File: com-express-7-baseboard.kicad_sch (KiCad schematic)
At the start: 0 parts

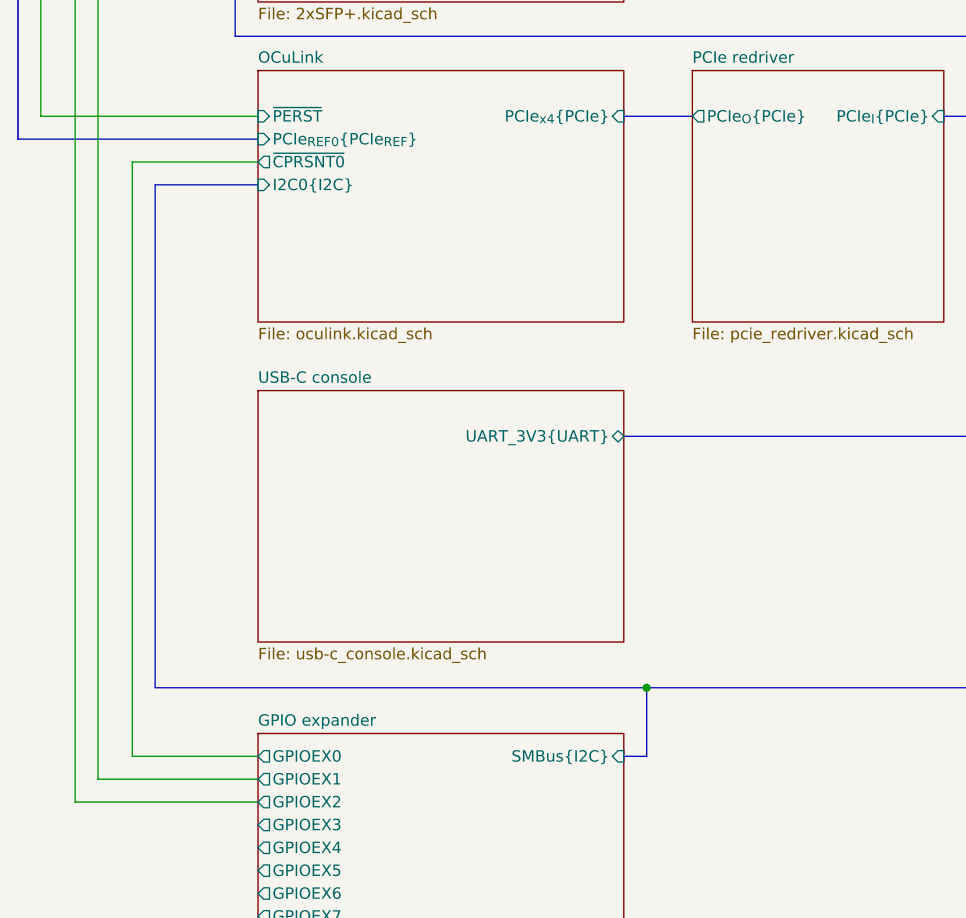
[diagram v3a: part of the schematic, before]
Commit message: [#57056] Add PCIe redriver for OCuLink
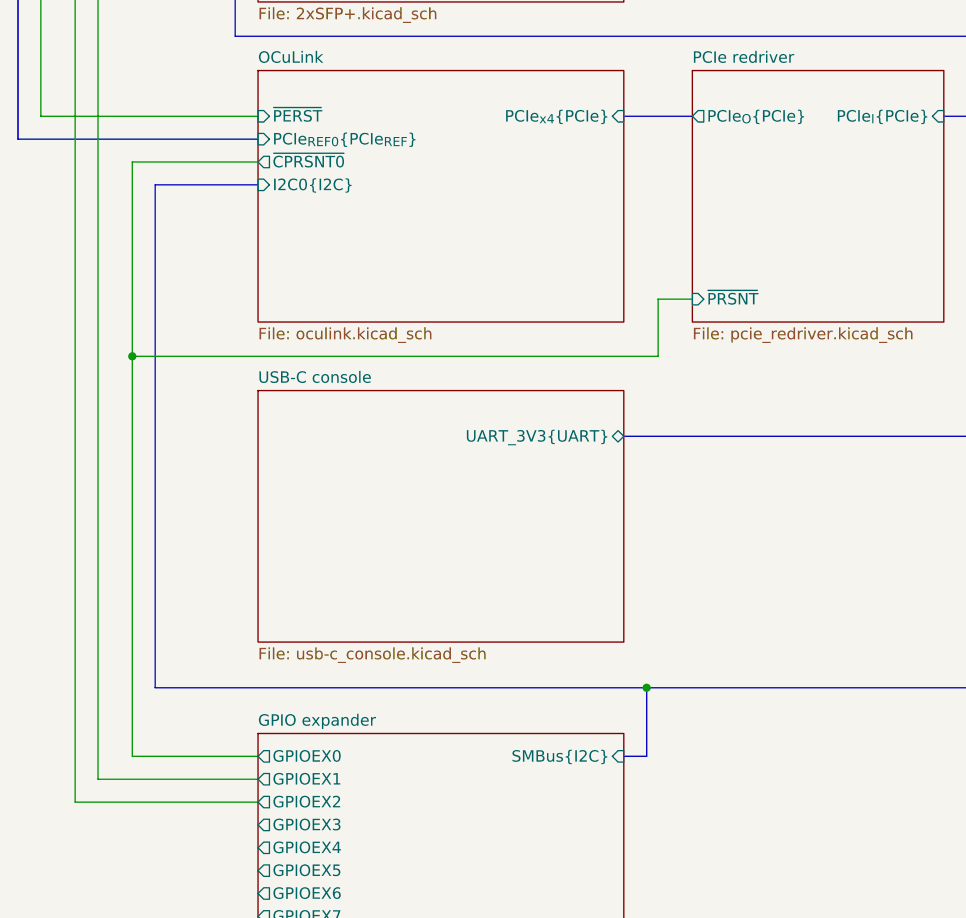
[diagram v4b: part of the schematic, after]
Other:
- sheet PCIe redriver ports: added ~{PRSNT}; removed none
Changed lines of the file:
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@@
   (junction (at 325.12 101.6) (diameter 0) (color 0 0 0 0)
+  )
+  (junction (at 64.77 171.45) (diameter 0) (color 0 0 0 0)
   )
   (junction (at 121.92 127) (diameter 0) (color 0 0 0 0)
@@
     (stroke (width 0) (type default))
   )
+  (wire (pts (xy 64.77 171.45) (xy 64.77 215.9))
+    (stroke (width 0) (type default))
+  )
   (bus (pts (xy 78.74 147.32) (xy 52.07 147.32))
     (stroke (width 0) (type default))
@@
     (stroke (width 0) (type default) (color 0 0 255 1))
   )
+  (wire (pts (xy 64.77 171.45) (xy 123.19 171.45))
+    (stroke (width 0) (type default))
+  )
   (bus (pts (xy 335.28 106.68) (xy 335.28 27.94))
     (stroke (width 0) (type default))
@@
     (stroke (width 0) (type default) (color 255 0 0 1))
   )
+  (wire (pts (xy 123.19 165.1) (xy 127 165.1))
+    (stroke (width 0) (type default))
+  )
   (wire (pts (xy 325.12 137.16) (xy 322.58 137.16))
     (stroke (width 0) (type default))
@@
     (stroke (width 0) (type default))
   )
+  (wire (pts (xy 123.19 171.45) (xy 123.19 165.1))
+    (stroke (width 0) (type default))
+  )
   (bus (pts (xy 119.38 215.9) (xy 121.92 215.9))
     (stroke (width 0) (type default))
@@
     (stroke (width 0) (type default))
   )
-  (wire (pts (xy 64.77 149.86) (xy 64.77 215.9))
+  (wire (pts (xy 64.77 149.86) (xy 64.77 171.45))
     (stroke (width 0) (type default))
   )
@@
       (effects (font (size 1.27 1.27)) (justify left))
     )
+    (pin "~{PRSNT}" input (at 127 165.1 180)
+      (effects (font (size 1.27 1.27)) (justify left))
+    )

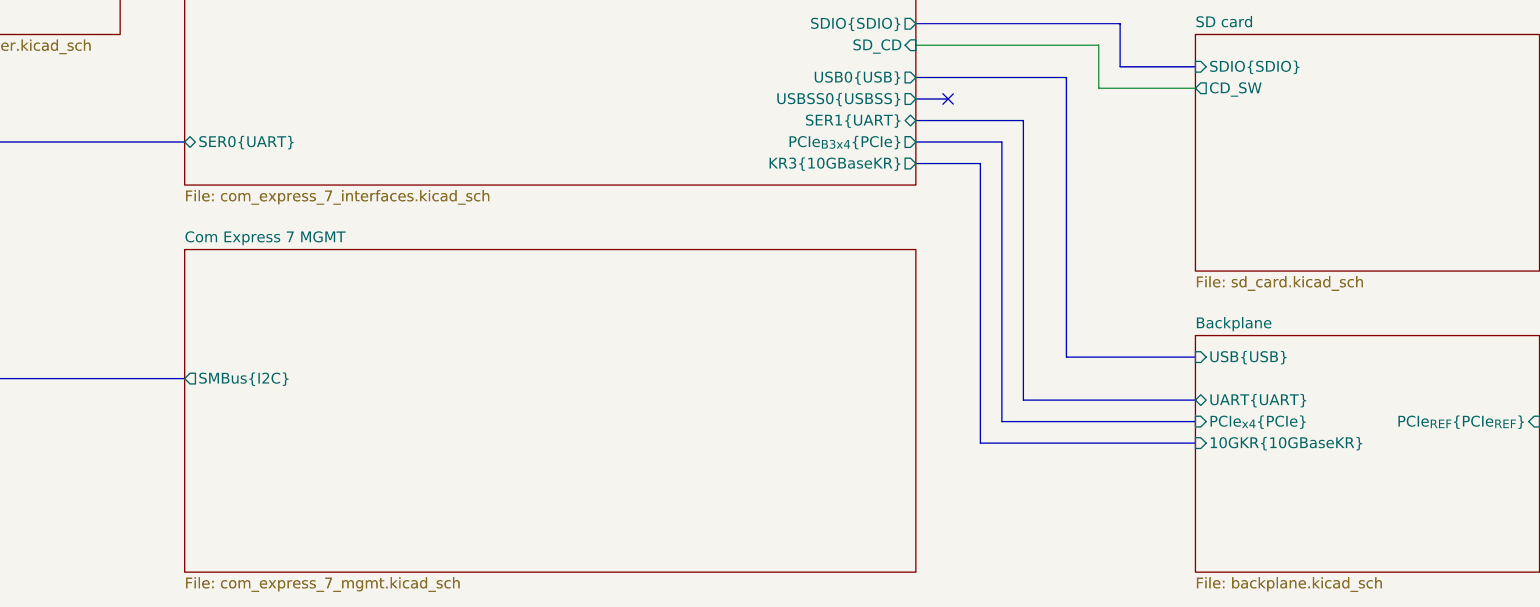
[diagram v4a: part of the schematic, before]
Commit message: [#57056] Add backplane connector
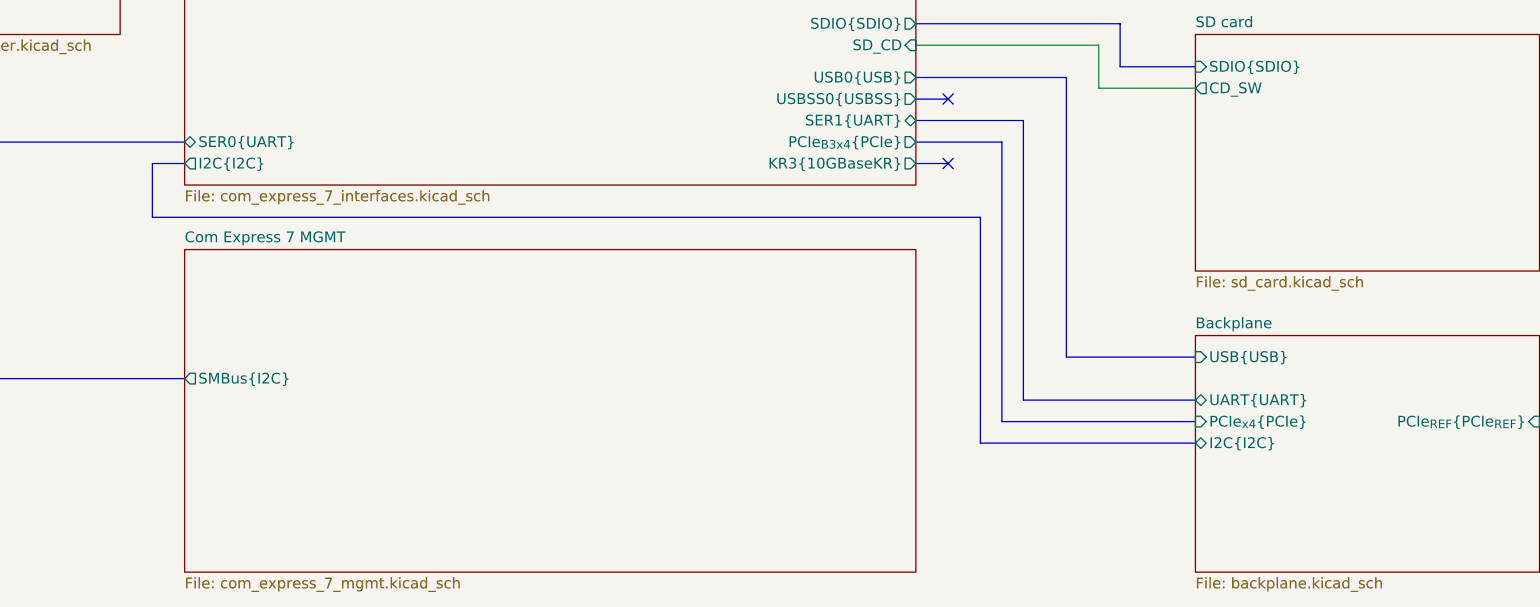
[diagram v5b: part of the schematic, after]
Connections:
- no-connect marks 3 -> 4
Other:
- sheet Backplane ports: added I2C{I2C}; removed 10GKR{10GBaseKR}
- sheet Com Express 7 Interfaces ports: added I2C{I2C}; removed none
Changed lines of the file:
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@@
   (no_connect (at 158.75 97.79))
   (no_connect (at 252.73 175.26))
+  (no_connect (at 252.73 182.88))
   (bus (pts (xy 261.62 210.82) (xy 281.94 210.82))
     (stroke (width 0) (type default) (color 255 153 0 1))
@@
     (stroke (width 0) (type default))
   )
-  (bus (pts (xy 256.54 215.9) (xy 281.94 215.9))
-    (stroke (width 0) (type default) (color 255 0 0 1))
-  )
   (wire (pts (xy 325.12 101.6) (xy 325.12 137.16))
     (stroke (width 0) (type default))
@@
     (stroke (width 0) (type default) (color 0 0 255 1))
   )
+  (bus (pts (xy 158.75 182.88) (xy 158.75 189.23))
+    (stroke (width 0) (type default))
+  )
   (wire (pts (xy 327.66 68.58) (xy 327.66 104.14))
     (stroke (width 0) (type default))
@@
     (stroke (width 0) (type default))
   )
+  (bus (pts (xy 162.56 182.88) (xy 158.75 182.88))
+    (stroke (width 0) (type default))
+  )
   (wire (pts (xy 322.58 101.6) (xy 325.12 101.6))
     (stroke (width 0) (type default))
@@
     (stroke (width 0) (type default) (color 194 0 194 1))
   )
+  (bus (pts (xy 256.54 189.23) (xy 256.54 215.9))
+    (stroke (width 0) (type default))
+  )
   (bus (pts (xy 52.07 22.86) (xy 52.07 147.32))
     (stroke (width 0) (type default))
@@
     (stroke (width 0) (type default))
   )
+  (bus (pts (xy 248.92 182.88) (xy 252.73 182.88))
+    (stroke (width 0) (type default))
+  )
   (bus (pts (xy 121.92 208.28) (xy 162.56 208.28))
     (stroke (width 0) (type default))
@@
     (stroke (width 0) (type default))
   )
+  (bus (pts (xy 158.75 189.23) (xy 256.54 189.23))
+    (stroke (width 0) (type default))
+  )
   (bus (pts (xy 273.05 171.45) (xy 281.94 171.45))
     (stroke (width 0) (type default))
@@
     (stroke (width 0) (type default))
   )
-  (bus (pts (xy 248.92 182.88) (xy 256.54 182.88))
-    (stroke (width 0) (type default) (color 255 0 0 1))
-  )
-  (bus (pts (xy 256.54 182.88) (xy 256.54 215.9))
-    (stroke (width 0) (type default) (color 255 0 0 1))
-  )
   (bus (pts (xy 254 35.56) (xy 261.62 35.56))
     (stroke (width 0) (type default))
@@
   )
   (bus (pts (xy 78.74 129.54) (xy 76.2 129.54))
+    (stroke (width 0) (type default))
+  )
+  (bus (pts (xy 256.54 215.9) (xy 281.94 215.9))
     (stroke (width 0) (type default))
   )
@@
       (effects (font (size 1.27 1.27)) (justify left))
     )
-    (pin "10GKR{10GBaseKR}" input (at 281.94 215.9 180)
-      (effects (font (size 1.27 1.27)) (justify left))
-    )
     (pin "PCIe_{x4}{PCIe}" input (at 281.94 213.36 180)
       (effects (font (size 1.27 1.27)) (justify left))
@@
       (effects (font (size 1.27 1.27)) (justify right))
     )
+    (pin "I2C{I2C}" bidirectional (at 281.94 215.9 180)
+      (effects (font (size 1.27 1.27)) (justify left))
+    )
     (instances
       (project "com-express-7-baseboard"
@@
       (effects (font (size 1.27 1.27)) (justify right))
     )
-    (instances
+    (pin "I2C{I2C}" output (at 162.56 182.88 180)
+      (effects (font (size 1.27 1.27)) (justify left))
+    )
+    (instances

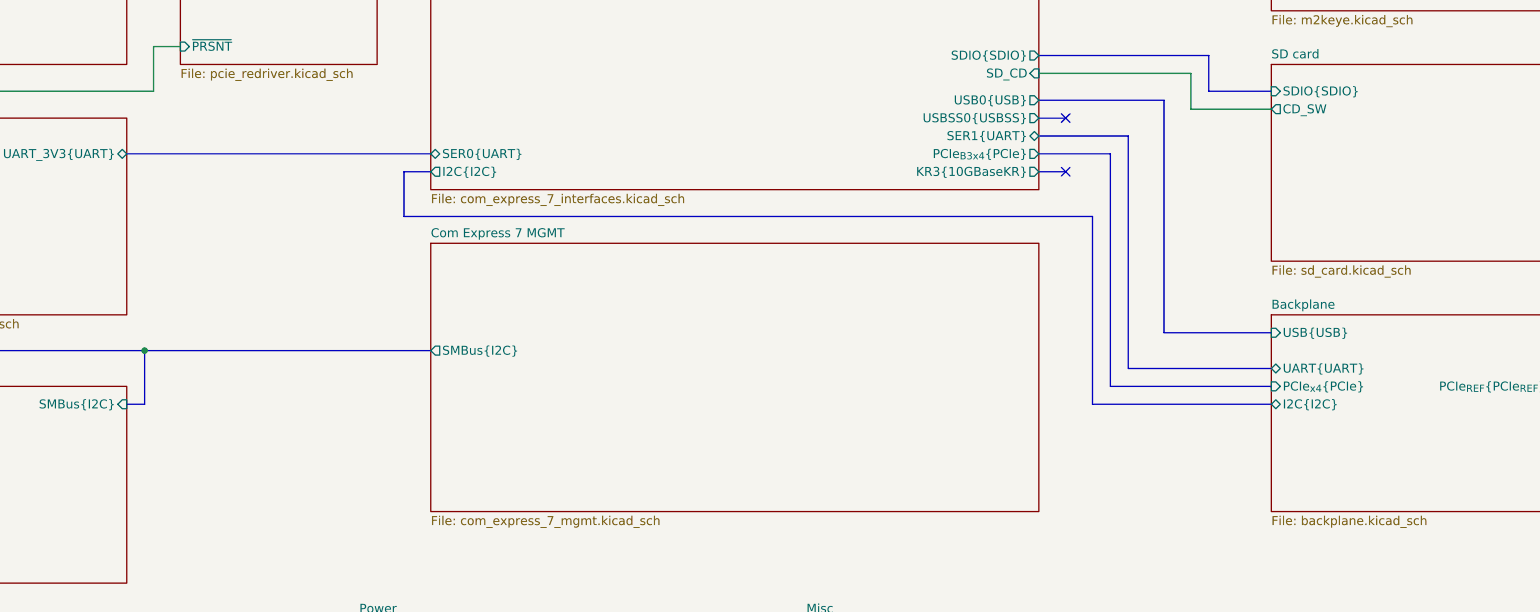
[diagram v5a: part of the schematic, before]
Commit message: [#57905] Add MAFS carrier BIOS
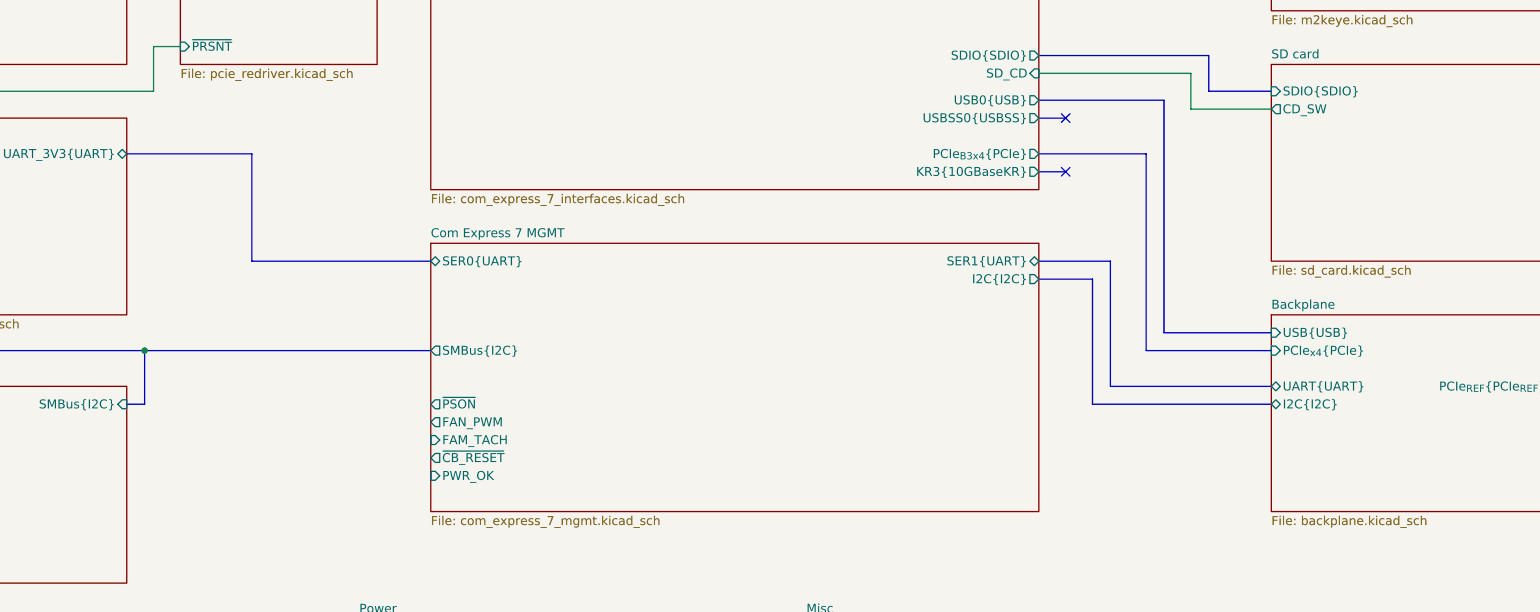
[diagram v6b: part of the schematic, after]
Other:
- sheet Com Express 7 Interfaces ports: added none; removed I2C{I2C}, SER0{UART}, SER1{UART}
- sheet Com Express 7 MGMT ports: added FAM_TACH, FAN_PWM, I2C{I2C}, PWR_OK, SER0{UART}, SER1{UART}, ~{CB_RESET}, ~{PSON}; removed none
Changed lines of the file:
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@@
   (no_connect (at 252.73 175.26))
   (no_connect (at 252.73 182.88))
-  (bus (pts (xy 261.62 210.82) (xy 281.94 210.82))
+  (bus (pts (xy 259.08 213.36) (xy 281.94 213.36))
     (stroke (width 0) (type default) (color 255 153 0 1))
   )
@@
     (stroke (width 0) (type default))
   )
+  (bus (pts (xy 259.08 195.58) (xy 259.08 213.36))
+    (stroke (width 0) (type default) (color 255 153 0 1))
+  )
   (wire (pts (xy 299.72 33.02) (xy 327.66 33.02))
     (stroke (width 0) (type default))
@@
     (stroke (width 0) (type default) (color 0 0 255 1))
   )
-  (bus (pts (xy 158.75 182.88) (xy 158.75 189.23))
-    (stroke (width 0) (type default))
-  )
   (wire (pts (xy 327.66 68.58) (xy 327.66 104.14))
     (stroke (width 0) (type default))
@@
   (bus (pts (xy 248.92 144.78) (xy 251.46 144.78))
     (stroke (width 0) (type default))
+  )
+  (bus (pts (xy 248.92 195.58) (xy 259.08 195.58))
+    (stroke (width 0) (type default) (color 255 153 0 1))
   )
   (bus (pts (xy 248.92 175.26) (xy 252.73 175.26))
@@
     (stroke (width 0) (type default))
   )
-  (bus (pts (xy 261.62 177.8) (xy 261.62 210.82))
-    (stroke (width 0) (type default) (color 255 153 0 1))
-  )
   (wire (pts (xy 119.38 86.36) (xy 121.92 86.36))
     (stroke (width 0) (type default))
@@
     (stroke (width 0) (type default))
   )
-  (bus (pts (xy 248.92 180.34) (xy 259.08 180.34))
+  (bus (pts (xy 248.92 180.34) (xy 264.16 180.34))
     (stroke (width 0) (type default) (color 194 0 194 1))
   )
@@
     (stroke (width 0) (type default))
   )
-  (bus (pts (xy 259.08 180.34) (xy 259.08 213.36))
+  (bus (pts (xy 264.16 180.34) (xy 264.16 208.28))
     (stroke (width 0) (type default) (color 194 0 194 1))
   )
@@
     (stroke (width 0) (type default))
   )
-  (bus (pts (xy 162.56 182.88) (xy 158.75 182.88))
-    (stroke (width 0) (type default))
-  )
   (wire (pts (xy 322.58 101.6) (xy 325.12 101.6))
     (stroke (width 0) (type default))
@@
     (stroke (width 0) (type default) (color 194 0 194 1))
   )
-  (bus (pts (xy 256.54 189.23) (xy 256.54 215.9))
-    (stroke (width 0) (type default))
-  )
   (bus (pts (xy 52.07 22.86) (xy 52.07 147.32))
     (stroke (width 0) (type default))
   )
+  (bus (pts (xy 162.56 195.58) (xy 137.16 195.58))
+    (stroke (width 0) (type default) (color 255 153 0 1))
+  )
   (bus (pts (xy 119.38 119.38) (xy 162.56 119.38))
     (stroke (width 0) (type default))
@@
     (stroke (width 0) (type default))
   )
+  (bus (pts (xy 137.16 195.58) (xy 137.16 180.34))
+    (stroke (width 0) (type default) (color 255 153 0 1))
+  )
   (wire (pts (xy 121.92 129.54) (xy 121.92 127))
     (stroke (width 0) (type default))
   )
   (bus (pts (xy 299.72 25.4) (xy 337.82 25.4))
+    (stroke (width 0) (type default))
+  )
+  (bus (pts (xy 248.92 198.12) (xy 256.54 198.12))
     (stroke (width 0) (type default))
   )
@@
     (stroke (width 0) (type default))
   )
-  (bus (pts (xy 119.38 180.34) (xy 162.56 180.34))
+  (bus (pts (xy 119.38 180.34) (xy 137.16 180.34))
     (stroke (width 0) (type default) (color 255 153 0 1))
   )
@@
     (stroke (width 0) (type default))
   )
-  (bus (pts (xy 248.92 177.8) (xy 261.62 177.8))
-    (stroke (width 0) (type default) (color 255 153 0 1))
-  )
   (wire (pts (xy 54.61 144.78) (xy 78.74 144.78))
     (stroke (width 0) (type default))
@@
     (stroke (width 0) (type default))
   )
-  (bus (pts (xy 158.75 189.23) (xy 256.54 189.23))
-    (stroke (width 0) (type default))
-  )
   (bus (pts (xy 273.05 171.45) (xy 281.94 171.45))
     (stroke (width 0) (type default))
@@
     (stroke (width 0) (type default))
   )
-  (bus (pts (xy 259.08 213.36) (xy 281.94 213.36))
+  (bus (pts (xy 264.16 208.28) (xy 281.94 208.28))
     (stroke (width 0) (type default) (color 194 0 194 1))
   )
@@
     (stroke (width 0) (type default) (color 255 0 0 1))
   )
+  (bus (pts (xy 256.54 198.12) (xy 256.54 215.9))
+    (stroke (width 0) (type default))
+  )
   (bus (pts (xy 266.7 172.72) (xy 266.7 205.74))
     (stroke (width 0) (type default) (color 0 0 255 1))
@@
       (effects (font (size 1.27 1.27)) (justify left))
     )
-    (pin "UART{UART}" bidirectional (at 281.94 210.82 180)
-      (effects (font (size 1.27 1.27)) (justify left))
-    )
-    (pin "PCIe_{x4}{PCIe}" input (at 281.94 213.36 180)
+    (pin "UART{UART}" bidirectional (at 281.94 213.36 180)
+      (effects (font (size 1.27 1.27)) (justify left))
+    )
+    (pin "PCIe_{x4}{PCIe}" input (at 281.94 208.28 180)
       (effects (font (size 1.27 1.27)) (justify left))
     )
@@
       (effects (font (size 1.27 1.27)) (justify right))
     )
-    (pin "SER0{UART}" bidirectional (at 162.56 180.34 180)
-      (effects (font (size 1.27 1.27)) (justify left))
-    )
-    (pin "SER1{UART}" bidirectional (at 248.92 177.8 0)
-      (effects (font (size 1.27 1.27)) (justify right))
-    )
     (pin "~{GBE0_ACT}" output (at 162.56 68.58 180)
       (effects (font (size 1.27 1.27)) (justify left))
@@
       (effects (font (size 1.27 1.27)) (justify right))
     )
-    (pin "I2C{I2C}" output (at 162.56 182.88 180)
-      (effects (font (size 1.27 1.27)) (justify left))
-    )
     (instances
       (project "com-express-7-baseboard"
@@
       (effects (font (size 1.27 1.27)) (justify left))
     )
-    (instances
+    (pin "~{PSON}" output (at 162.56 215.9 180)
+      (effects (font (size 1.27 1.27)) (justify left))
+    )
+    (pin "FAN_PWM" output (at 162.56 218.44 180)
+      (effects (font (size 1.27 1.27)) (justify left))
+    )
+    (pin "FAM_TACH" input (at 162.56 220.98 180)
+      (effects (font (size 1.27 1.27)) (justify left))
+    )
+    (pin "~{CB_RESET}" output (at 162.56 223.52 180)
+      (effects (font (size 1.27 1.27)) (justify left))
+    )
+    (pin "PWR_OK" input (at 162.56 226.06 180)
+      (effects (font (size 1.27 1.27)) (justify left))
+    )
+    (pin "I2C{I2C}" output (at 248.92 198.12 0)
+      (effects (font (size 1.27 1.27)) (justify right))
+    )
+    (pin "SER0{UART}" bidirectional (at 162.56 195.58 180)
+      (effects (font (size 1.27 1.27)) (justify left))
+    )
+    (pin "SER1{UART}" bidirectional (at 248.92 195.58 0)
+      (effects (font (size 1.27 1.27)) (justify right))
+    )
+    (instances
